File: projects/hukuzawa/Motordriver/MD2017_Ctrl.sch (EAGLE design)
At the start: 14 parts, among them IC1 PIC16F648, J1 3X2A, Q1 CERALOCK

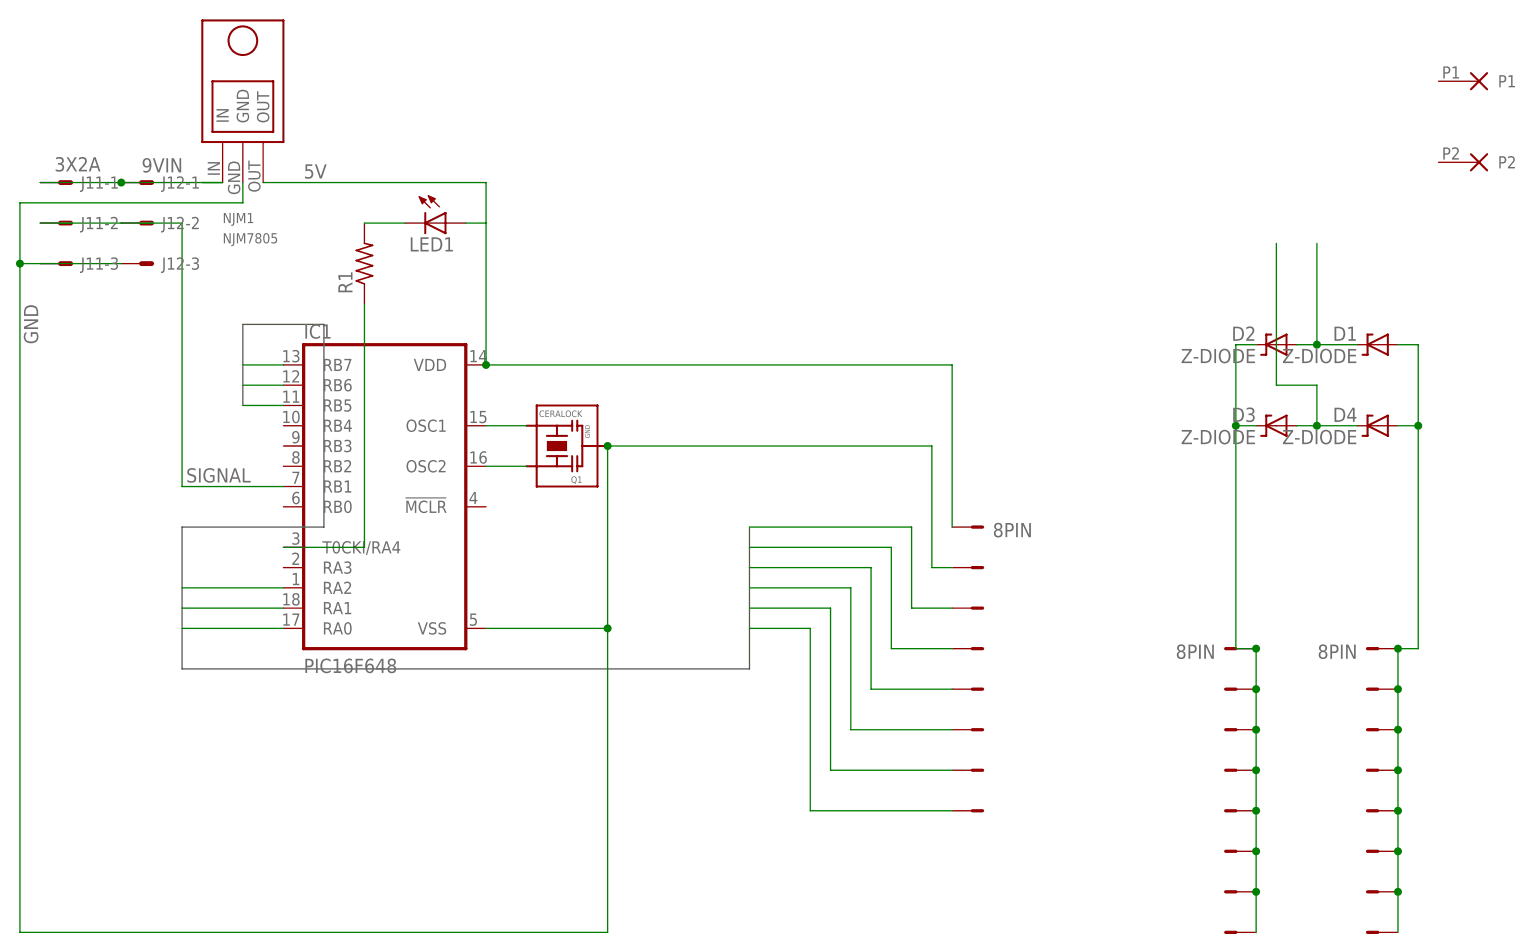
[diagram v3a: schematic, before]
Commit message: モータードライバ制御部回路図完成
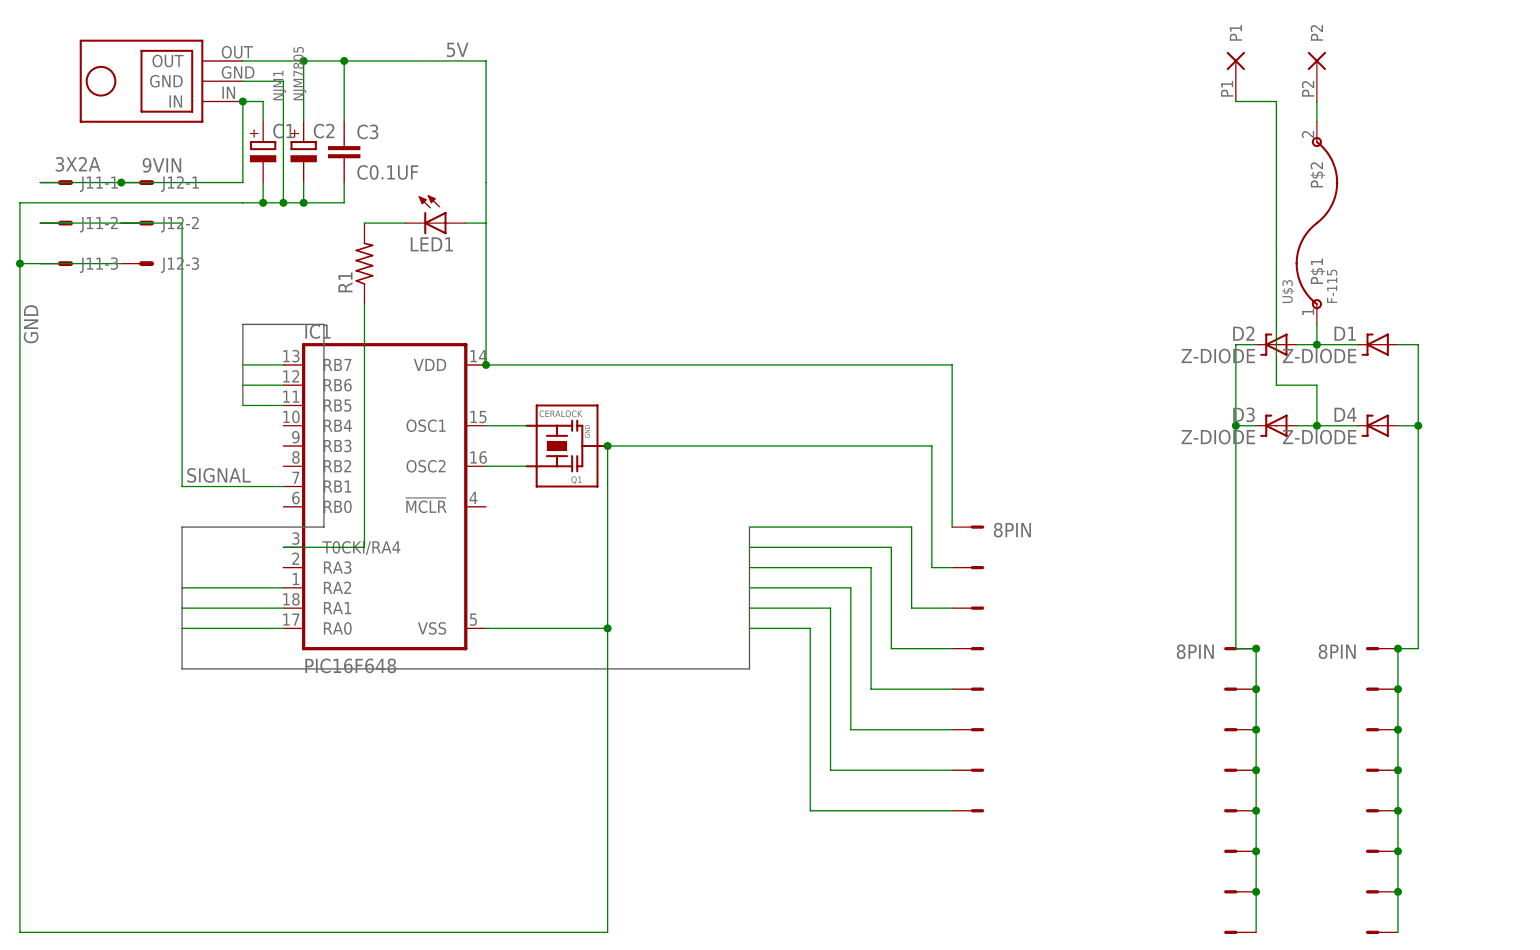
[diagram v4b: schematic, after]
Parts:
- added C1, C2: (no value), FP-21T for MITS:CPOL-EU2-5MM
- added C3: C0.1UF, FP-21T for MITS:C0.1UF
- added U$3: F-115, testLib:F-115
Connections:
- new net N$4: U$2.P2, U$3.P$2
- net 5V: now also C2.+, C3.1
- net 9VIN: now also C1.+
- net GND: now also C1.-, C2.-, C3.2
- net N$5: now also U$3.P$1
- net N$6: now also U$2.P1
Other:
- moved on the sheet: NJM1
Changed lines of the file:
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@@
 <part name="R1" library="rcl" deviceset="R-US_" device="R3216W"/>
 <part name="U$2" library="Powerio" deviceset="2P" device=""/>
+<part name="U$3" library="testLib" deviceset="F-115" device=""/>
+<part name="C1" library="FP-21T for MITS" deviceset="CPOL-EU2" device="-5MM"/>
+<part name="C2" library="FP-21T for MITS" deviceset="CPOL-EU2" device="-5MM"/>
+<part name="C3" library="FP-21T for MITS" deviceset="C0.1UF" device=""/>
 </parts>
 <sheets>
@@
 <instance part="IC1" gate="G$1" x="-48.26" y="0"/>
 <instance part="Q1" gate="G$1" x="-25.4" y="5.08" rot="R90"/>
-<instance part="NJM1" gate="G$1" x="-66.04" y="48.26"/>
+<instance part="NJM1" gate="G$1" x="-76.2" y="50.8" rot="R90"/>
 <instance part="U$1" gate="-3" x="27.94" y="-15.24"/>
 <instance part="U$1" gate="-4" x="27.94" y="-20.32"/>
@@
 <instance part="LED1" gate="G$1" x="-40.64" y="33.02" rot="R270"/>
 <instance part="R1" gate="G$1" x="-50.8" y="27.94" rot="R90"/>
-<instance part="U$2" gate="G1" x="88.9" y="45.72" rot="R270"/>
+<instance part="U$2" gate="G1" x="63.5" y="53.34"/>
+<instance part="U$3" gate="G$1" x="68.58" y="33.02" rot="R90"/>
+<instance part="C1" gate="G$1" x="-63.5" y="43.18"/>
+<instance part="C2" gate="G$1" x="-58.42" y="43.18"/>
+<instance part="C3" gate="G$1" x="-53.34" y="40.64"/>
 </instances>
 <busses>
@@
 <net name="5V" class="0">
 <segment>
-<pinref part="NJM1" gate="G$1" pin="OUT"/>
 <pinref part="IC1" gate="G$1" pin="VDD"/>
-<wire x1="-63.5" y1="38.1" x2="-35.56" y2="38.1" width="0.1524" layer="91"/>
 <wire x1="-35.56" y1="38.1" x2="-35.56" y2="33.02" width="0.1524" layer="91"/>
-<label x="-58.42" y="38.608" size="1.778" layer="95"/>
+<label x="-40.64" y="53.848" size="1.778" layer="95"/>
 <pinref part="LED1" gate="G$1" pin="A"/>
 <wire x1="-35.56" y1="33.02" x2="-35.56" y2="15.24" width="0.1524" layer="91"/>
@@
 <wire x1="22.86" y1="15.24" x2="22.86" y2="-5.08" width="0.1524" layer="91"/>
 <junction x="-35.56" y="15.24"/>
+<pinref part="NJM1" gate="G$1" pin="OUT"/>
+<wire x1="-66.04" y1="53.34" x2="-58.42" y2="53.34" width="0.1524" layer="91"/>
+<wire x1="-58.42" y1="53.34" x2="-53.34" y2="53.34" width="0.1524" layer="91"/>
+<wire x1="-53.34" y1="53.34" x2="-35.56" y2="53.34" width="0.1524" layer="91"/>
+<wire x1="-35.56" y1="53.34" x2="-35.56" y2="38.1" width="0.1524" layer="91"/>
+<pinref part="C2" gate="G$1" pin="+"/>
+<wire x1="-58.42" y1="53.34" x2="-58.42" y2="45.72" width="0.1524" layer="91"/>
+<junction x="-58.42" y="53.34"/>
+<pinref part="C3" gate="G$1" pin="1"/>
+<wire x1="-53.34" y1="45.72" x2="-53.34" y2="53.34" width="0.1524" layer="91"/>
+<junction x="-53.34" y="53.34"/>
 </segment>
 </net>
 <net name="9VIN" class="0">
 <segment>
-<pinref part="NJM1" gate="G$1" pin="IN"/>
-<wire x1="-71.12" y1="38.1" x2="-68.58" y2="38.1" width="0.1524" layer="91"/>
 <pinref part="J1" gate="1-1" pin="S"/>
 <wire x1="-91.44" y1="38.1" x2="-81.28" y2="38.1" width="0.1524" layer="91"/>
 <label x="-78.74" y="39.37" size="1.778" layer="95"/>
 <pinref part="J1" gate="2-1" pin="S"/>
+<pinref part="NJM1" gate="G$1" pin="IN"/>
+<wire x1="-81.28" y1="38.1" x2="-66.04" y2="38.1" width="0.1524" layer="91"/>
+<wire x1="-66.04" y1="38.1" x2="-66.04" y2="48.26" width="0.1524" layer="91"/>
 <junction x="-81.28" y="38.1"/>
-<wire x1="-81.28" y1="38.1" x2="-68.58" y2="38.1" width="0.1524" layer="91"/>
+<pinref part="C1" gate="G$1" pin="+"/>
+<wire x1="-66.04" y1="48.26" x2="-63.5" y2="48.26" width="0.1524" layer="91"/>
+<wire x1="-63.5" y1="48.26" x2="-63.5" y2="45.72" width="0.1524" layer="91"/>
+<junction x="-66.04" y="48.26"/>
 </segment>
 </net>
@@
 <net name="GND" class="0">
 <segment>
-<pinref part="NJM1" gate="G$1" pin="GND"/>
-<wire x1="-66.04" y1="38.1" x2="-66.04" y2="35.56" width="0.1524" layer="91"/>
 <wire x1="-66.04" y1="35.56" x2="-93.98" y2="35.56" width="0.1524" layer="91"/>
 <wire x1="-93.98" y1="35.56" x2="-93.98" y2="27.94" width="0.1524" layer="91"/>
@@
 <junction x="-20.32" y="-17.78"/>
 <junction x="-93.98" y="27.94"/>
+<wire x1="-66.04" y1="35.56" x2="-63.5" y2="35.56" width="0.1524" layer="91"/>
+<wire x1="-63.5" y1="35.56" x2="-60.96" y2="35.56" width="0.1524" layer="91"/>
+<wire x1="-60.96" y1="35.56" x2="-60.96" y2="50.8" width="0.1524" layer="91"/>
+<pinref part="NJM1" gate="G$1" pin="GND"/>
+<wire x1="-60.96" y1="50.8" x2="-66.04" y2="50.8" width="0.1524" layer="91"/>
+<pinref part="C1" gate="G$1" pin="-"/>
+<wire x1="-63.5" y1="38.1" x2="-63.5" y2="35.56" width="0.1524" layer="91"/>
+<junction x="-63.5" y="35.56"/>
+<pinref part="C2" gate="G$1" pin="-"/>
+<wire x1="-58.42" y1="38.1" x2="-58.42" y2="35.56" width="0.1524" layer="91"/>
+<pinref part="C3" gate="G$1" pin="2"/>
+<wire x1="-58.42" y1="35.56" x2="-53.34" y2="35.56" width="0.1524" layer="91"/>
+<wire x1="-53.34" y1="35.56" x2="-53.34" y2="38.1" width="0.1524" layer="91"/>
+<wire x1="-58.42" y1="35.56" x2="-60.96" y2="35.56" width="0.1524" layer="91"/>
+<junction x="-58.42" y="35.56"/>
+<junction x="-60.96" y="35.56"/>
 </segment>
 </net>
@@
 <wire x1="73.66" y1="17.78" x2="68.58" y2="17.78" width="0.1524" layer="91"/>
 <wire x1="68.58" y1="17.78" x2="66.04" y2="17.78" width="0.1524" layer="91"/>
-<wire x1="68.58" y1="17.78" x2="68.58" y2="30.48" width="0.1524" layer="91"/>
+<wire x1="68.58" y1="17.78" x2="68.58" y2="20.32" width="0.1524" layer="91"/>
 <junction x="68.58" y="17.78"/>
+<pinref part="U$3" gate="G$1" pin="P$1"/>
 </segment>
 </net>
@@
 <wire x1="68.58" y1="12.7" x2="63.5" y2="12.7" width="0.1524" layer="91"/>
 <wire x1="63.5" y1="12.7" x2="63.5" y2="30.48" width="0.1524" layer="91"/>
+<pinref part="U$2" gate="G1" pin="P1"/>
+<wire x1="58.42" y1="48.26" x2="63.5" y2="48.26" width="0.1524" layer="91"/>
+<wire x1="63.5" y1="48.26" x2="63.5" y2="30.48" width="0.1524" layer="91"/>
 </segment>
 </net>
@@
 </segment>
 </net>
+<net name="N$4" class="0">
+<segment>
+<pinref part="U$3" gate="G$1" pin="P$2"/>
+<pinref part="U$2" gate="G1" pin="P2"/>
+<wire x1="68.58" y1="45.72" x2="68.58" y2="48.26" width="0.1524" layer="91"/>
+</segment>
+</net>

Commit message: モータードライバボード図2枚一時完成
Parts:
- renumbered U$1 to SIGNALPORT
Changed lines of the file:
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@@
 <part name="Q1" library="FP-21T for MITS" deviceset="CERALOCK" device=""/>
 <part name="NJM1" library="My_NJM7805" deviceset="NJM7805" device=""/>
-<part name="U$1" library="FH105" deviceset="8PIN" device=""/>
+<part name="SIGNALPORT" library="FH105" deviceset="8PIN" device=""/>
 <part name="POWERNPORT" library="FH105" deviceset="8PIN" device=""/>
 <part name="POWERPPORT" library="FH105" deviceset="8PIN" device=""/>
@@
 <instance part="Q1" gate="G$1" x="-25.4" y="5.08" rot="R90"/>
 <instance part="NJM1" gate="G$1" x="-76.2" y="50.8" rot="R90"/>
-<instance part="U$1" gate="-3" x="27.94" y="-15.24"/>
-<instance part="U$1" gate="-4" x="27.94" y="-20.32"/>
-<instance part="U$1" gate="-5" x="27.94" y="-25.4"/>
-<instance part="U$1" gate="-6" x="27.94" y="-30.48"/>
-<instance part="U$1" gate="-2" x="27.94" y="-10.16"/>
-<instance part="U$1" gate="-8" x="27.94" y="-40.64"/>
-<instance part="U$1" gate="-7" x="27.94" y="-35.56"/>
-<instance part="U$1" gate="-1" x="27.94" y="-5.08"/>
+<instance part="SIGNALPORT" gate="-3" x="27.94" y="-15.24"/>
+<instance part="SIGNALPORT" gate="-4" x="27.94" y="-20.32"/>
+<instance part="SIGNALPORT" gate="-5" x="27.94" y="-25.4"/>
+<instance part="SIGNALPORT" gate="-6" x="27.94" y="-30.48"/>
+<instance part="SIGNALPORT" gate="-2" x="27.94" y="-10.16"/>
+<instance part="SIGNALPORT" gate="-8" x="27.94" y="-40.64"/>
+<instance part="SIGNALPORT" gate="-7" x="27.94" y="-35.56"/>
+<instance part="SIGNALPORT" gate="-1" x="27.94" y="-5.08"/>
 <instance part="POWERNPORT" gate="-3" x="73.66" y="-30.48" rot="MR0"/>
 <instance part="POWERNPORT" gate="-4" x="73.66" y="-35.56" rot="MR0"/>
@@
 <wire x1="-35.56" y1="33.02" x2="-35.56" y2="15.24" width="0.1524" layer="91"/>
 <wire x1="-38.1" y1="33.02" x2="-35.56" y2="33.02" width="0.1524" layer="91"/>
-<pinref part="U$1" gate="-1" pin="P$1"/>
+<pinref part="SIGNALPORT" gate="-1" pin="P$1"/>
 <wire x1="-35.56" y1="15.24" x2="22.86" y2="15.24" width="0.1524" layer="91"/>
 <wire x1="22.86" y1="15.24" x2="22.86" y2="-5.08" width="0.1524" layer="91"/>
@@
 <wire x1="-53.34" y1="45.72" x2="-53.34" y2="53.34" width="0.1524" layer="91"/>
 <junction x="-53.34" y="53.34"/>
+<junction x="-35.56" y="33.02"/>
 </segment>
 </net>
@@
 <wire x1="20.32" y1="5.08" x2="20.32" y2="-10.16" width="0.1524" layer="91"/>
 <junction x="-20.32" y="5.08"/>
-<pinref part="U$1" gate="-2" pin="P$1"/>
+<pinref part="SIGNALPORT" gate="-2" pin="P$1"/>
 <wire x1="20.32" y1="-10.16" x2="22.86" y2="-10.16" width="0.1524" layer="91"/>
 <junction x="-20.32" y="-17.78"/>
@@
 <wire x1="-2.54" y1="-5.08" x2="17.78" y2="-5.08" width="0.1524" layer="91"/>
 <wire x1="17.78" y1="-5.08" x2="17.78" y2="-15.24" width="0.1524" layer="91"/>
-<pinref part="U$1" gate="-3" pin="P$1"/>
+<pinref part="SIGNALPORT" gate="-3" pin="P$1"/>
 <wire x1="17.78" y1="-15.24" x2="22.86" y2="-15.24" width="0.1524" layer="91"/>
 </segment>
@@
 <wire x1="-2.54" y1="-7.62" x2="15.24" y2="-7.62" width="0.1524" layer="91"/>
 <wire x1="15.24" y1="-7.62" x2="15.24" y2="-20.32" width="0.1524" layer="91"/>
-<pinref part="U$1" gate="-4" pin="P$1"/>
+<pinref part="SIGNALPORT" gate="-4" pin="P$1"/>
 <wire x1="15.24" y1="-20.32" x2="22.86" y2="-20.32" width="0.1524" layer="91"/>
 </segment>
@@
 <wire x1="-2.54" y1="-10.16" x2="12.7" y2="-10.16" width="0.1524" layer="91"/>
 <wire x1="12.7" y1="-10.16" x2="12.7" y2="-25.4" width="0.1524" layer="91"/>
-<pinref part="U$1" gate="-5" pin="P$1"/>
+<pinref part="SIGNALPORT" gate="-5" pin="P$1"/>
 <wire x1="12.7" y1="-25.4" x2="22.86" y2="-25.4" width="0.1524" layer="91"/>
 </segment>
@@
 <wire x1="-2.54" y1="-12.7" x2="10.16" y2="-12.7" width="0.1524" layer="91"/>
 <wire x1="10.16" y1="-12.7" x2="10.16" y2="-30.48" width="0.1524" layer="91"/>
-<pinref part="U$1" gate="-6" pin="P$1"/>
+<pinref part="SIGNALPORT" gate="-6" pin="P$1"/>
 <wire x1="10.16" y1="-30.48" x2="22.86" y2="-30.48" width="0.1524" layer="91"/>
 </segment>
@@
 <wire x1="-2.54" y1="-15.24" x2="7.62" y2="-15.24" width="0.1524" layer="91"/>
 <wire x1="7.62" y1="-15.24" x2="7.62" y2="-35.56" width="0.1524" layer="91"/>
-<pinref part="U$1" gate="-7" pin="P$1"/>
+<pinref part="SIGNALPORT" gate="-7" pin="P$1"/>
 <wire x1="7.62" y1="-35.56" x2="22.86" y2="-35.56" width="0.1524" layer="91"/>
 </segment>
@@
 <wire x1="-2.54" y1="-17.78" x2="5.08" y2="-17.78" width="0.1524" layer="91"/>
 <wire x1="5.08" y1="-17.78" x2="5.08" y2="-40.64" width="0.1524" layer="91"/>
-<pinref part="U$1" gate="-8" pin="P$1"/>
+<pinref part="SIGNALPORT" gate="-8" pin="P$1"/>
 <wire x1="5.08" y1="-40.64" x2="22.86" y2="-40.64" width="0.1524" layer="91"/>
 </segment>

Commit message: モータードライバ修正
穴径を1.0～1.2mmの範囲に収まるよう修正
Dimensionラインの太さを0に修正
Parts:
- D1, D2, D3, D4: device FP-21T for MITS:Z-DIODE -> diode:Z-DIODE
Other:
- moved on the sheet: D1, D2, D3, D4
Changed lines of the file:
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@@
 <part name="POWERPPORT" library="FH105" deviceset="8PIN" device=""/>
 <part name="J1" library="3M_372xx" deviceset="3X2" device="A"/>
-<part name="D1" library="FP-21T for MITS" deviceset="Z-DIODE" device=""/>
-<part name="D2" library="FP-21T for MITS" deviceset="Z-DIODE" device=""/>
-<part name="D3" library="FP-21T for MITS" deviceset="Z-DIODE" device=""/>
-<part name="D4" library="FP-21T for MITS" deviceset="Z-DIODE" device=""/>
 <part name="LED1" library="FP-21T for MITS" deviceset="LED" device="5MM"/>
 <part name="R1" library="rcl" deviceset="R-US_" device="R3216W"/>
@@
 <part name="C2" library="FP-21T for MITS" deviceset="CPOL-EU2" device="-5MM"/>
 <part name="C3" library="FP-21T for MITS" deviceset="C0.1UF" device=""/>
+<part name="D1" library="diode" deviceset="Z-DIODE" device=""/>
+<part name="D2" library="diode" deviceset="Z-DIODE" device=""/>
+<part name="D3" library="diode" deviceset="Z-DIODE" device=""/>
+<part name="D4" library="diode" deviceset="Z-DIODE" device=""/>
 </parts>
 <sheets>
@@
 <instance part="J1" gate="2-2" x="-76.2" y="33.02"/>
 <instance part="J1" gate="2-3" x="-76.2" y="27.94"/>
-<instance part="D1" gate="1" x="76.2" y="17.78" rot="MR0"/>
-<instance part="D2" gate="1" x="63.5" y="17.78" rot="MR0"/>
-<instance part="D3" gate="1" x="63.5" y="7.62" rot="MR0"/>
-<instance part="D4" gate="1" x="76.2" y="7.62" rot="MR0"/>
 <instance part="LED1" gate="G$1" x="-40.64" y="33.02" rot="R270"/>
 <instance part="R1" gate="G$1" x="-50.8" y="27.94" rot="R90"/>
@@
 <instance part="C2" gate="G$1" x="-58.42" y="43.18"/>
 <instance part="C3" gate="G$1" x="-53.34" y="40.64"/>
+<instance part="D1" gate="1" x="76.2" y="17.78" rot="R180"/>
+<instance part="D2" gate="1" x="63.5" y="17.78" rot="R180"/>
+<instance part="D3" gate="1" x="63.5" y="7.62" rot="R180"/>
+<instance part="D4" gate="1" x="76.2" y="7.62" rot="R180"/>
 </instances>
 <busses>
@@
 <net name="N$3" class="0">
 <segment>
-<pinref part="D1" gate="1" pin="A"/>
 <wire x1="78.74" y1="17.78" x2="81.28" y2="17.78" width="0.1524" layer="91"/>
 <wire x1="81.28" y1="17.78" x2="81.28" y2="7.62" width="0.1524" layer="91"/>
-<pinref part="D4" gate="1" pin="A"/>
 <wire x1="81.28" y1="7.62" x2="78.74" y2="7.62" width="0.1524" layer="91"/>
 <wire x1="81.28" y1="7.62" x2="81.28" y2="-20.32" width="0.1524" layer="91"/>
@@
 <junction x="78.74" y="-50.8"/>
 <wire x1="78.74" y1="-50.8" x2="78.74" y2="-55.88" width="0.1524" layer="91"/>
+<pinref part="D1" gate="1" pin="A"/>
+<pinref part="D4" gate="1" pin="A"/>
 </segment>
 </net>
 <net name="N$5" class="0">
 <segment>
-<pinref part="D1" gate="1" pin="C"/>
-<pinref part="D2" gate="1" pin="A"/>
 <wire x1="73.66" y1="17.78" x2="68.58" y2="17.78" width="0.1524" layer="91"/>
 <wire x1="68.58" y1="17.78" x2="66.04" y2="17.78" width="0.1524" layer="91"/>
@@
 <junction x="68.58" y="17.78"/>
 <pinref part="U$3" gate="G$1" pin="P$1"/>
+<pinref part="D1" gate="1" pin="C"/>
+<pinref part="D2" gate="1" pin="A"/>
 </segment>
 </net>
 <net name="N$6" class="0">
 <segment>
-<pinref part="D4" gate="1" pin="C"/>
-<pinref part="D3" gate="1" pin="A"/>
 <wire x1="73.66" y1="7.62" x2="68.58" y2="7.62" width="0.1524" layer="91"/>
 <wire x1="68.58" y1="7.62" x2="66.04" y2="7.62" width="0.1524" layer="91"/>
@@
 <wire x1="58.42" y1="48.26" x2="63.5" y2="48.26" width="0.1524" layer="91"/>
 <wire x1="63.5" y1="48.26" x2="63.5" y2="30.48" width="0.1524" layer="91"/>
+<pinref part="D3" gate="1" pin="A"/>
+<pinref part="D4" gate="1" pin="C"/>
 </segment>
 </net>
@@
 <pinref part="POWERPPORT" gate="-1" pin="P$1"/>
 <wire x1="60.96" y1="-55.88" x2="60.96" y2="-50.8" width="0.1524" layer="91"/>
-<pinref part="D2" gate="1" pin="C"/>
 <wire x1="60.96" y1="-50.8" x2="60.96" y2="-45.72" width="0.1524" layer="91"/>
 <wire x1="60.96" y1="-45.72" x2="60.96" y2="-40.64" width="0.1524" layer="91"/>
@@
 <wire x1="60.96" y1="17.78" x2="58.42" y2="17.78" width="0.1524" layer="91"/>
 <wire x1="58.42" y1="17.78" x2="58.42" y2="7.62" width="0.1524" layer="91"/>
-<pinref part="D3" gate="1" pin="C"/>
 <wire x1="58.42" y1="7.62" x2="60.96" y2="7.62" width="0.1524" layer="91"/>
 <wire x1="60.96" y1="-20.32" x2="58.42" y2="-20.32" width="0.1524" layer="91"/>
@@
 <pinref part="POWERPPORT" gate="-7" pin="P$1"/>
 <junction x="60.96" y="-50.8"/>
-</segment>
-</net>
+<pinref part="D2" gate="1" pin="C"/>
+<pinref part="D3" gate="1" pin="C"/>
+</segment>
+</net>
